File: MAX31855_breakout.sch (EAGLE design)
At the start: 17 parts, among them IC1 MAX31855, IC2 LP298XS, J1 1X2-3.5MM

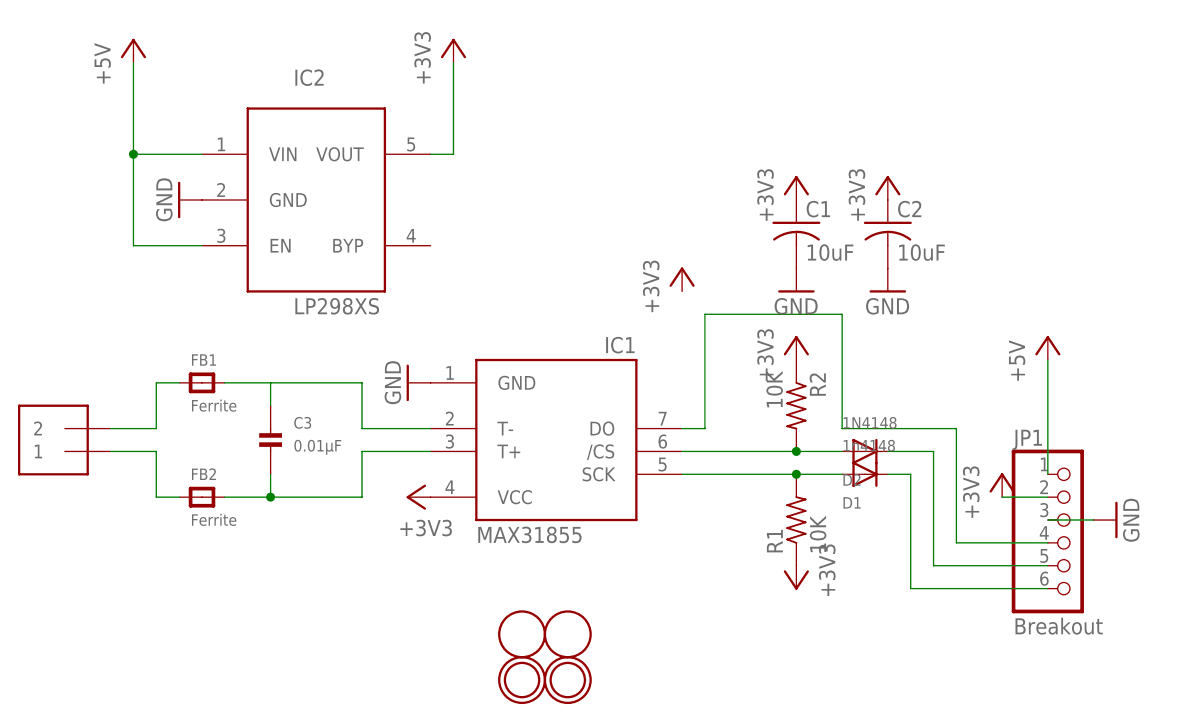
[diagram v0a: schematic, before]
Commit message: modifications to Adafruit MAX31855 breakout v2 for OSHpark
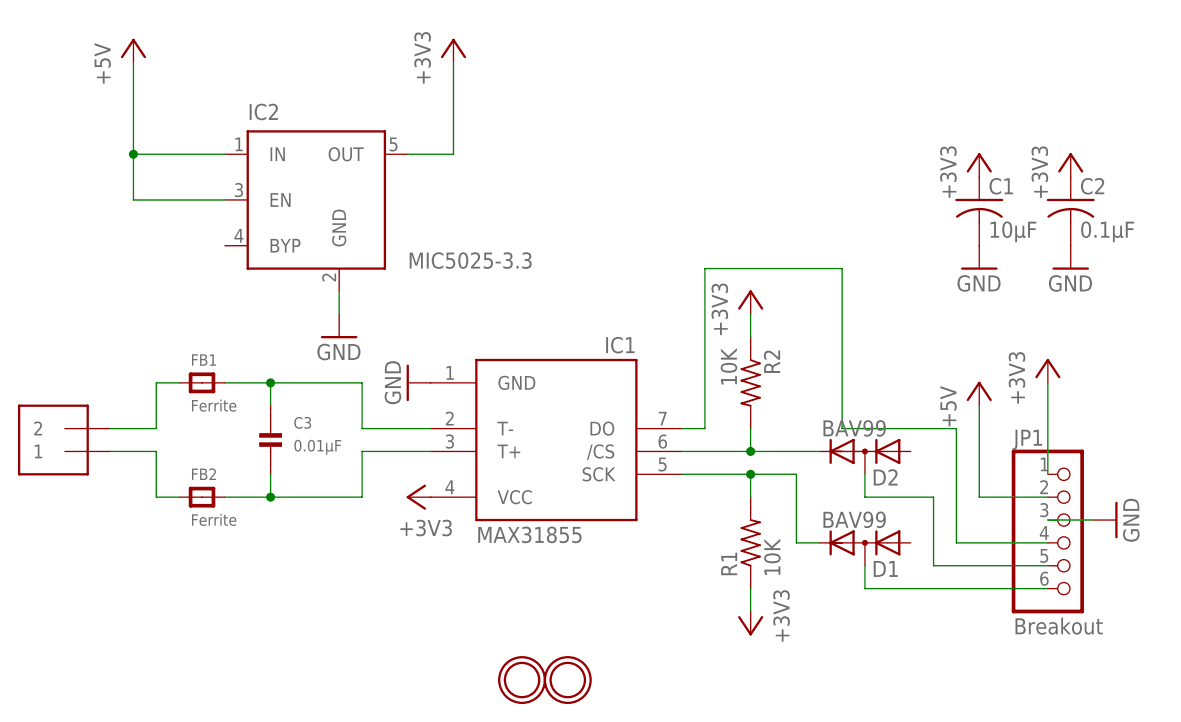
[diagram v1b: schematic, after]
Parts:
- removed U$1, U$2: FIDUCIAL, adafruit:FIDUCIAL
- C1: value 10uF -> 10µF
- C2: value 10uF -> 0.1µF
- D1: value 1n4148 -> BAV99; device adafruit:DIODESOD-323F -> diode:BAV199
- D2: value 1N4148 -> BAV99; device adafruit:DIODESOD-323F -> diode:BAV199
- IC2: value LP298XS -> MIC5025-3.3; device adafruit:LP298XS -> v-reg-micrel:MIC5219XX
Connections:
- removed net CS: D2.A, IC1./CS, R2.2
- new net N$7: D2.C, IC1./CS, R2.2
- net +3V3: now also IC2.OUT, JP1.1; no longer IC2.VOUT, JP1.2
- net +5V: now also IC2.IN, JP1.2; no longer IC2.VIN, JP1.1
- net N$2: now also D2.AC; no longer D2.C
- net N$3: now also D1.AC; no longer D1.C
- net SCK: now also D1.C; no longer D1.A
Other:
- moved on the sheet: C1, C2, R1, R2
